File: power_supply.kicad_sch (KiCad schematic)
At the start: 17 parts, among them J10 CONN_01X02, J11 CONN_01X02, J8 USB_C_Receptacle_Power_Only, J9 5V, Q1 ZXMP6A13FTA, SW1 SW_SPDT, U10 MCP73831, U11 DC-DC-Boost-Converter-Positiv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

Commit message: holes, jst bat, ..
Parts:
- J10: footprint Connector_PinHeader_2.54mm:PinHeader_1x02_P2.54mm_Vertical -> Connector_JST:JST_PH_S2B-PH-K_1x02_P2.00mm_Horizontal
- J8: value USB_C_Receptacle_Power_Only -> UJC-HP-3-SMT-TR
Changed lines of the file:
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@@
     (property "Reference" "J10" (id 0) (at 146.05 109.22 0))
     (property "Value" "CONN_01X02" (id 1) (at 142.24 111.76 90))
-    (property "Footprint" "Connector_PinHeader_2.54mm:PinHeader_1x02_P2.54mm_Vertical" (id 2) (at 142.24 109.22 0)
+    (property "Footprint" "Connector_JST:JST_PH_S2B-PH-K_1x02_P2.00mm_Horizontal" (id 2) (at 142.24 109.22 0)
       (effects (font (size 1.27 1.27)) hide)
     )
@@
   (symbol (lib_id "stahllabs:USB_C_Receptacle_Power_Only") (at 34.29 100.33 0) (unit 1)
     (in_bom yes) (on_board yes)
-    (property "Reference" "J8" (id 0) (at 37.0078 78.3082 0))
-    (property "Value" "USB_C_Receptacle_Power_Only" (id 1) (at 37.0078 80.6196 0))
+    (property "Reference" "J8" (id 0) (at 34.29 78.74 0))
+    (property "Value" "UJC-HP-3-SMT-TR" (id 1) (at 34.29 81.28 0))
     (property "Footprint" "stahllabs:USB_C_Receptacle_CUI_Devices_UJC-HP-3-SMT-TR" (id 2) (at 34.29 76.2 0)
       (effects (font (size 1.27 1.27)) hide)

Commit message: documentation / update kicad
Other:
- note added: "Power-On switch"
- moved on the sheet: C49, C50, D2, J10, J11, Q1, R67, SW1

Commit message: update LICENSE
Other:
- company: (none) -> stahllabs
- title: (none) -> mixerli

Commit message: added erratum for pull-down resistors
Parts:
- D1, D3: footprint LEDs:LED_D3.0mm -> LED_THT:LED_Rectangular_W5.0mm_H2.0mm
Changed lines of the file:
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@@
       (effects (font (size 1.27 1.27)))
     )
-    (property "Footprint" "LEDs:LED_D3.0mm" (at 88.9 116.84 0)
+    (property "Footprint" "LED_THT:LED_Rectangular_W5.0mm_H2.0mm" (at 88.9 116.84 0)
       (effects (font (size 1.27 1.27)) hide)
     )
@@
       (effects (font (size 1.27 1.27)))
     )
-    (property "Footprint" "LEDs:LED_D3.0mm" (at 212.09 115.57 0)
+    (property "Footprint" "LED_THT:LED_Rectangular_W5.0mm_H2.0mm" (at 212.09 115.57 0)
       (effects (font (size 1.27 1.27)) hide)
     )
@@
   (symbol (lib_id "power:GND") (at 144.78 127 0) (unit 1)
     (in_bom yes) (on_board yes) (dnp no)
-    (property "Reference" "#PWR?" (at 144.78 133.35 0)
+    (property "Reference" "#PWR0123" (at 144.78 133.35 0)
       (effects (font (size 1.27 1.27)) hide)
     )
@@
       (project "mixerli"
         (path "/4f411f68-04bd-4175-a406-bcaa4cf6601e/00000000-0000-0000-0000-00005940313f"
-          (reference "#PWR?") (unit 1)
-        )
-      )
+          (reference "#PWR0123") (unit 1)
+        )
+      )

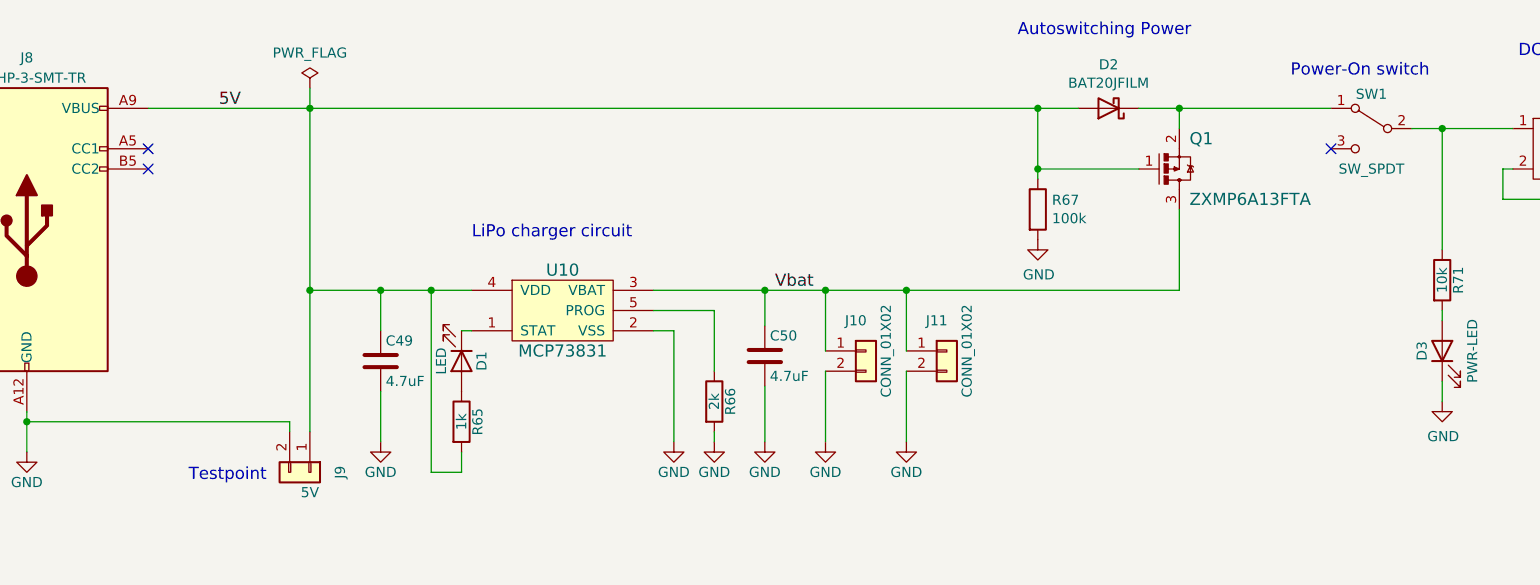
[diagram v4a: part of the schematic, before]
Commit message: v2.0.1: fixed pulldown resistors
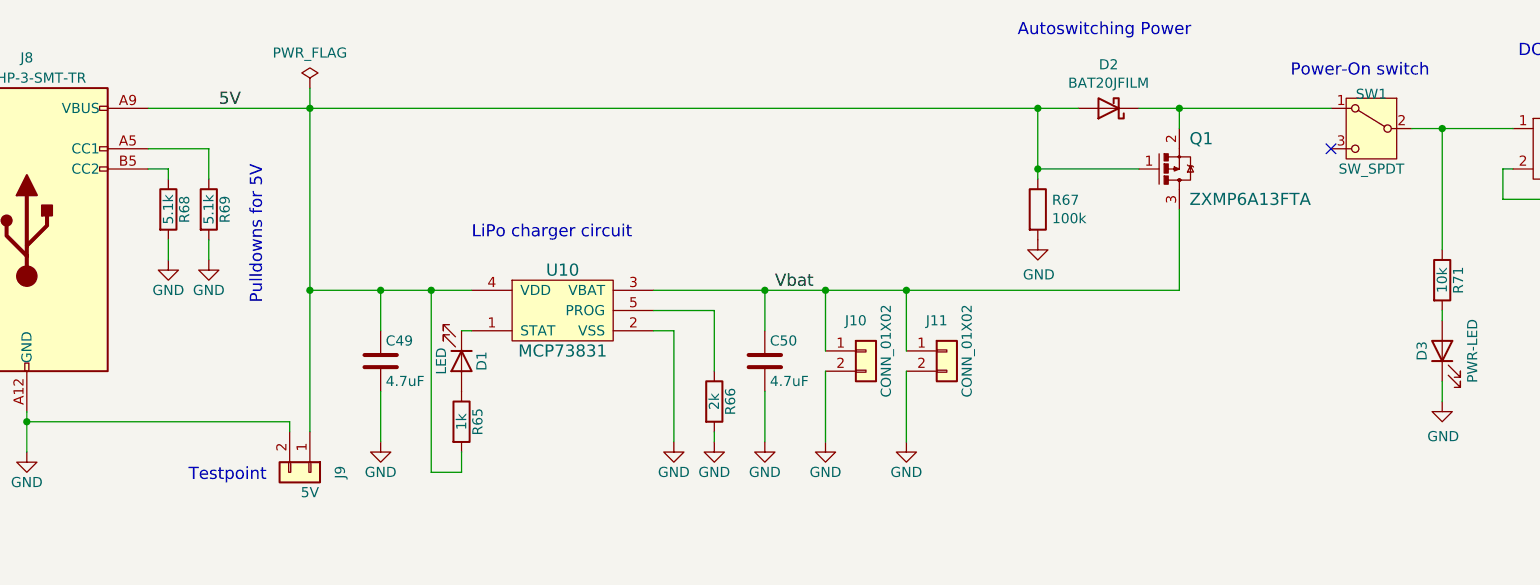
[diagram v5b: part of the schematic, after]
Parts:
- added R68, R69: 5.1k, Resistor_SMD:R_1206_3216Metric, symbol Device:R
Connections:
- net GND: now also R68.2, R69.2
- net at J8.A5 (CC1): now also R69.1
- net at J8.B5 (CC2): now also R68.1
- no-connect marks 4 -> 2
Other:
- note added: "Pulldowns for 5V"
- moved on the sheet: C50
